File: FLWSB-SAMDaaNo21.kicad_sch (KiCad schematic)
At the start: 29 parts

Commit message: Schema zo goed als af
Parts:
- added D6: D_Schottky, symbol Device:D_Schottky
- added J2: DEBUG, symbol Connector_Generic:Conn_01x03
- added R5, R6: 4.7k, symbol Device:R
- added TP2: VBUS, symbol Connector:TestPoint
- added TP3: VDD, symbol Connector:TestPoint
- added TP4: VIN, symbol Connector:TestPoint
- added TP5: TestPoint, symbol Connector:TestPoint
- J3, J4: renamed from J?; symbol Connector:Conn_01x15_Male -> Connector_Generic:Conn_01x15
- SW1: renamed from SW?; value SW_Push -> SW_RESET
- gave numbers to parts that had none: 26
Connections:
- net 3.3V is gone; now on net +3V3: C4.1, U1.2 (VO)
- net +3V3: now also J3.2 (Pin_2), R5.1, R6.1, TP3.1; no longer J3.14 (Pin_14)
- net GND: now also J3.3 (Pin_3), J4.15 (Pin_15); no longer J3.15 (Pin_15)
- net RESET: now also J2.3 (Pin_3); no longer J3.3 (Pin_3)
- net SERCOM0_PAD0_TX: now also J4.14 (Pin_14); no longer J4.1 (Pin_1)
- net SERCOM0_PAD1_RX: now also J4.13 (Pin_13); no longer J4.2 (Pin_2)
- net SERCOM2_PAD1_TX: now also J4.12 (Pin_12); no longer J4.3 (Pin_3)
- net SERCOM2_PAD2_RX: now also J4.11 (Pin_11); no longer J4.4 (Pin_4)
- net SERCOM3_MISO: now also J4.6 (Pin_6); no longer J4.9 (Pin_9)
- net SERCOM3_MOSI: now also J4.5 (Pin_5); no longer J4.10 (Pin_10)
- net SERCOM3_SCK: now also J4.4 (Pin_4); no longer J4.11 (Pin_11)
- net SERCOM4_PAD0_SDA: now also J4.8 (Pin_8), R5.2; no longer J4.7 (Pin_7)
- net SERCOM4_PAD1_SCL: now also J4.7 (Pin_7), R6.2; no longer J4.8 (Pin_8)
- net SERCOM5_PAD0_TX: now also J4.10 (Pin_10); no longer J4.5 (Pin_5)
- net SERCOM5_PAD1_RX: now also J4.9 (Pin_9); no longer J4.6 (Pin_6)
- net SWCLK: now also J2.1 (Pin_1); no longer J3.1 (Pin_1)
- net SWDIO: now also J2.2 (Pin_2); no longer J3.2 (Pin_2)
- net PA02: now reaches J3.13 (Pin_13)
- net PA02: now also U2.3 (PA02)
- net at U2.39 (PA27): now also TP5.1
- net PB02: now reaches U2.47 (PB02)
- net PB02: now also J3.15 (Pin_15)
- net PB03: now reaches U2.48 (PB03)
- net PB03: now also J3.14 (Pin_14)
- net A0 renamed PA10
- net PA10: now also J3.9 (Pin_9); no longer J4.12 (Pin_12)
- net A1 renamed PA11
- net PA11: now also J3.8 (Pin_8); no longer J4.13 (Pin_13)
- net A2 renamed PA19
- net PA19: now also J3.5 (Pin_5); no longer J4.14 (Pin_14)
- net ADC_0 renamed PA20
- net PA20: now also U2.29 (PA20); no longer U2.3 (PA02)
- net D0 renamed PA03
- net PA03: now also J3.12 (Pin_12); no longer J3.9 (Pin_9)
- net D1 renamed PA09
- net D2 renamed PA06
- net PA06: now also U2.11 (PA06); no longer U2.29 (PA20)
- net D3 renamed PA21
- net PA21: now also J4.1 (Pin_1); no longer J3.12 (Pin_12)
- net PWM0_WO0 renamed PA14
- net PA14: now also J3.7 (Pin_7); no longer J3.5 (Pin_5)
- net PWM0_WO1 renamed PA15
- net PWM1_WO0 renamed PB08
- net PB08: now also J4.2 (Pin_2); no longer J3.7 (Pin_7)
- net PWM1_WO1 renamed PB09
- net PB09: now also J4.3 (Pin_3); no longer J3.8 (Pin_8)
- removed net RN2483_RESET: J4.15 (Pin_15), U2.11 (PA06)
- net VBUS_5V renamed VBUS
- net VBUS: now also D6.2 (A), TP2.1; no longer C1.1, U1.3 (VI)
- new net VIN: C1.1, D6.1 (K), J3.1 (Pin_1), TP4.1, U1.3 (VI)
- no-connect marks 13 -> 10
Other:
- note added: "Input / Ouput"
- note added: "Low Dropout Lineair Regulator"
- note added: "Power Supply Connections"
- note added: "RESET & DEBUG"
- note added: "USB Interface & VIN"
- company: (none) -> AP-Hogeschool
- title: (none) -> Flexible LoRaWAN Sensor Board ATSAMD21
- moved on the sheet: C1, C10, C11, C12, C2, C4, C5, C6, C7, C8, C9, L1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

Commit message: PCB bijna af
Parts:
- removed TP5: TestPoint, symbol Connector:TestPoint
- C3: footprint (none) -> Capacitor_SMD:C_0805_2012Metric_Pad1.18x1.45mm_HandSolder
- D1, D2, D3, D4, D5, R4, R5, R6: footprint (none) -> Resistor_SMD:R_0805_2012Metric_Pad1.20x1.40mm_HandSolder
- D6: footprint (none) -> footprints:SOD-123FL
- J1: footprint USB4085-GF-A_REVA4:GCT_USB4085-GF-A_REVA4 -> footprints:GCT_USB4085-GF-A_REVA4
- J2: footprint (none) -> Connector_PinHeader_2.54mm:PinHeader_1x03_P2.54mm_Vertical
- J3, J4: footprint (none) -> Connector_PinHeader_2.54mm:PinHeader_1x15_P2.54mm_Vertical
- TP1: renamed from TP2; footprint (none) -> TestPoint:TestPoint_Pad_D1.0mm
- TP2: renamed from TP3; footprint (none) -> TestPoint:TestPoint_Pad_D1.0mm
- TP3: renamed from TP4; footprint (none) -> TestPoint:TestPoint_Pad_D1.0mm
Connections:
- net PA02: now also J4.14 (Pin_14); no longer J3.13 (Pin_13)
- net PA03: now also J4.13 (Pin_13); no longer J3.12 (Pin_12)
- net PA06: now also J4.8 (Pin_8); no longer J3.11 (Pin_11)
- net PA09: now also J4.7 (Pin_7); no longer J3.10 (Pin_10)
- net PA10: now also J4.4 (Pin_4); no longer J3.9 (Pin_9)
- net PA11: now also J4.3 (Pin_3); no longer J3.8 (Pin_8)
- net PA14: now also J3.15 (Pin_15); no longer J3.7 (Pin_7)
- net PA15: now also J3.14 (Pin_14); no longer J3.6 (Pin_6)
- net PA19: now also J3.10 (Pin_10); no longer J3.5 (Pin_5)
- net PA20: now also J3.9 (Pin_9); no longer J3.4 (Pin_4)
- net PA21: now also J3.8 (Pin_8); no longer J4.1 (Pin_1)
- net PB03: now also J3.4 (Pin_4); no longer J3.14 (Pin_14)
- net PB08: now also J4.12 (Pin_12); no longer J4.2 (Pin_2)
- net PB09: now also J4.11 (Pin_11); no longer J4.3 (Pin_3)
- net SERCOM0_PAD0_TX: now also J4.10 (Pin_10); no longer J4.14 (Pin_14)
- net SERCOM0_PAD1_RX: now also J4.9 (Pin_9); no longer J4.13 (Pin_13)
- net SERCOM2_PAD1_TX: now also J4.6 (Pin_6); no longer J4.12 (Pin_12)
- net SERCOM2_PAD2_RX: now also J4.5 (Pin_5); no longer J4.11 (Pin_11)
- net SERCOM3_MISO: now also J3.11 (Pin_11); no longer J4.6 (Pin_6)
- net SERCOM3_MOSI: now also J3.13 (Pin_13); no longer J4.5 (Pin_5)
- net SERCOM3_SCK: now also J3.12 (Pin_12); no longer J4.4 (Pin_4)
- net SERCOM4_PAD0_SDA: now also J4.2 (Pin_2); no longer J4.8 (Pin_8)
- net SERCOM4_PAD1_SCL: now also J4.1 (Pin_1); no longer J4.7 (Pin_7)
- net SERCOM5_PAD0_TX: now also J3.7 (Pin_7); no longer J4.10 (Pin_10)
- net SERCOM5_PAD1_RX: now also J3.6 (Pin_6); no longer J4.9 (Pin_9)
- net PB22: now reaches U2.37 (PB22)
- net PB22: now also J3.5 (Pin_5)
- net PB02: no longer names the net of U2.47 (PB02)
- net PB02: no longer J3.15 (Pin_15)
- no-connect marks 10 -> 11

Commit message: Laatste verbeteringen
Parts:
- removed D1, D2, D3, D4, D5: D_Zener, Resistor_SMD:R_0805_2012Metric_Pad1.20x1.40mm_HandSolder, symbol Device:D_Zener
- added C13: 1µF, Capacitor_SMD:C_0805_2012Metric_Pad1.18x1.45mm_HandSolder, symbol Device:C_Small
- added D1: PRTR5V0U2X, Package_TO_SOT_SMD:SOT-143, symbol Power_Protection:PRTR5V0U2X
- added J6: Conn_Coaxial, Connector_Coaxial:U.FL_Molex_MCRF_73412-0110_Vertical, symbol Connector:Conn_Coaxial
- added U3: RN2483, RN2483:RN2483, symbol RN2483:RN2483
- SW1: footprint Button_Switch_SMD:SW_Push_1P1T_NO_6x6mm_H9.5mm -> KMR7_CNK:KMR7_CNK; symbol Switch:SW_Push -> KMR221G-LFS:KMR731NGLFS
- TP1, TP2, TP3: footprint TestPoint:TestPoint_Pad_D1.0mm -> TestPoint:TestPoint_THTPad_1.0x1.0mm_Drill0.5mm
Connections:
- net +3V3: now also C13.2, U3.12 (VDD_1), U3.34 (VDD_2)
- net GND: now also C13.1, D1.1 (GND), J6.2 (Ext), U3.1 (GND_1), U3.11 (GND_3), U3.20 (GND_4), U3.21 (GND_5), U3.22 (GND_6), U3.24 (GND_7), U3.26 (GND_8), U3.27 (GND_9), U3.28 (GND_10), U3.33 (GND_11), U3.41 (GND_12), U3.47 (GND_13), U3.8 (GND_2)
- net SERCOM2_PAD1_TX: now also U3.6 (UART_TX)
- net SERCOM2_PAD2_RX: now also U3.7 (UART_RX)
- net USB+: now also D1.3 (I/O2)
- net USB-: now also D1.2 (I/O1)
- net VBUS: now also D1.4 (VCC)
- net at SW1.1: no longer R1.1
- net PA09 renamed PA07
- net PA10 renamed RN2483_RESET
- net RN2483_RESET: now also U3.32 (~{RESET})
- new net: R1.1, SW1.4
- new net 868MHz: J6.1 (In), U3.23 (RFH)
- no-connect marks 11 -> 41
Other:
- moved on the sheet: C10, C11, C12, C2, C3, C7, C8, C9, D6, J1, L1, R1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

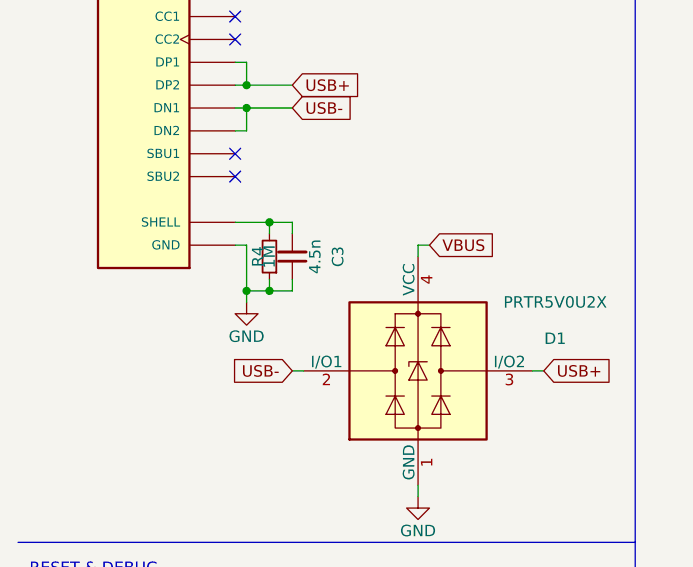
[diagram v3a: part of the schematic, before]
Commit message: USB-C shell aan GND ipv R en C
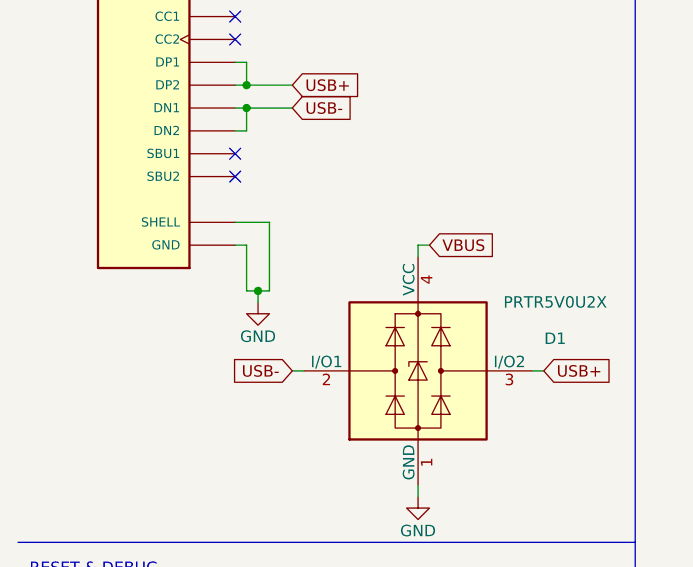
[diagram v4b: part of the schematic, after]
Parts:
- removed C3: 4.5n, Capacitor_SMD:C_0805_2012Metric_Pad1.18x1.45mm_HandSolder, symbol Device:C_Small
- removed R4: 1M, Resistor_SMD:R_0805_2012Metric_Pad1.20x1.40mm_HandSolder, symbol Device:R_Small
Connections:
- net GND: now also J1.P1 (SHELL), J1.P2 (SHELL), J1.P3 (SHELL), J1.P4 (SHELL)
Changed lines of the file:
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@@
     (comment 1 "Bavo, Birk, Daan")
   )
-  (junction (at 39.37 59.69) (diameter 0) (color 0 0 0 0)
-  )
   (junction (at 132.08 161.29) (diameter 0) (color 0 0 0 0)
   )
+  (junction (at 38.1 59.69) (diameter 0) (color 0 0 0 0)
+  )
   (junction (at 62.23 24.13) (diameter 0) (color 0 0 0 0)
   )
@@
   (junction (at 158.75 30.48) (diameter 0) (color 0 0 0 0)
   )
-  (junction (at 39.37 52.07) (diameter 0) (color 0 0 0 0)
-  )
   (junction (at 132.08 27.94) (diameter 0) (color 0 0 0 0)
   )
@@
   )
   (junction (at 166.37 60.96) (diameter 0) (color 0 0 0 0)
-  )
-  (junction (at 36.83 59.69) (diameter 0) (color 0 0 0 0)
   )
   (junction (at 64.77 111.76) (diameter 0) (color 0 0 0 0)
@@
     (stroke (width 0) (type default) (color 0 0 0 0))
   )
-  (wire (pts (xy 41.91 58.42) (xy 41.91 59.69))
-    (stroke (width 0) (type default) (color 0 0 0 0))
-  )
   (wire (pts (xy 33.02 137.16) (xy 34.29 137.16))
     (stroke (width 0) (type default) (color 0 0 0 0))
@@
     (stroke (width 0) (type default) (color 0 0 0 0))
   )
+  (wire (pts (xy 38.1 59.69) (xy 36.83 59.69))
+    (stroke (width 0) (type default) (color 0 0 0 0))
+  )
   (wire (pts (xy 55.88 111.76) (xy 54.61 111.76))
     (stroke (width 0) (type default) (color 0 0 0 0))
@@
     (stroke (width 0) (type default) (color 0 0 0 0))
   )
-  (wire (pts (xy 39.37 52.07) (xy 39.37 53.34))
-    (stroke (width 0) (type default) (color 0 0 0 0))
-  )
-  (wire (pts (xy 39.37 59.69) (xy 36.83 59.69))
+  (wire (pts (xy 39.37 59.69) (xy 38.1 59.69))
     (stroke (width 0) (type default) (color 0 0 0 0))
   )
@@
     (stroke (width 0) (type default) (color 0 0 0 0))
   )
+  (wire (pts (xy 39.37 52.07) (xy 39.37 59.69))
+    (stroke (width 0) (type default) (color 0 0 0 0))
+  )
   (wire (pts (xy 111.76 129.54) (xy 113.03 129.54))
     (stroke (width 0) (type default) (color 0 0 0 0))
@@
     (stroke (width 0) (type default) (color 0 0 0 0))
   )
-  (wire (pts (xy 36.83 59.69) (xy 36.83 60.96))
-    (stroke (width 0) (type default) (color 0 0 0 0))
-  )
   (wire (pts (xy 35.56 52.07) (xy 39.37 52.07))
     (stroke (width 0) (type default) (color 0 0 0 0))
@@
     (stroke (width 0) (type default) (color 0 0 0 0))
   )
-  (wire (pts (xy 41.91 59.69) (xy 39.37 59.69))
-    (stroke (width 0) (type default) (color 0 0 0 0))
-  )
   (wire (pts (xy 22.86 135.89) (xy 22.86 137.16))
     (stroke (width 0) (type default) (color 0 0 0 0))
@@
     (stroke (width 0) (type default) (color 0 0 0 0))
   )
+  (wire (pts (xy 38.1 59.69) (xy 38.1 60.96))
+    (stroke (width 0) (type default) (color 0 0 0 0))
+  )
   (wire (pts (xy 62.23 24.13) (xy 64.77 24.13))
     (stroke (width 0) (type default) (color 0 0 0 0))
@@
     (stroke (width 0) (type default) (color 0 0 0 0))
   )
-  (wire (pts (xy 39.37 52.07) (xy 41.91 52.07))
-    (stroke (width 0) (type default) (color 0 0 0 0))
-  )
   (wire (pts (xy 223.52 77.47) (xy 227.33 77.47))
     (stroke (width 0) (type default) (color 0 0 0 0))
@@
   )
   (polyline (pts (xy 175.26 165.1) (xy 175.26 101.6))
-    (stroke (width 0) (type default) (color 0 0 0 0))
-  )
-  (wire (pts (xy 41.91 52.07) (xy 41.91 53.34))
-    (stroke (width 0) (type default) (color 0 0 0 0))
-  )
-  (wire (pts (xy 39.37 58.42) (xy 39.37 59.69))
     (stroke (width 0) (type default) (color 0 0 0 0))
   )
@@
     )
     (pin "1")
-  )
-  (symbol (lib_id "Device:R_Small") (at 39.37 55.88 180) (unit 1)
-    (in_bom yes) (on_board yes)
-    (property "Reference" "R4" (id 0) (at 38.1 55.88 90))
-    (property "Value" "1M" (id 1) (at 39.37 55.88 90))
-    (property "Footprint" "Resistor_SMD:R_0805_2012Metric_Pad1.20x1.40mm_HandSolder" (id 2) (at 39.37 55.88 0)
-      (effects (font (size 1.27 1.27)) hide)
-    )
-    (property "Datasheet" "~" (id 3) (at 39.37 55.88 0)
-      (effects (font (size 1.27 1.27)) hide)
-    )
-    (pin "1")
-    (pin "2")
   )
   (symbol (lib_id "Device:C_Small") (at 179.07 49.53 180) (unit 1)
@@
     (pin "1")
   )
-  (symbol (lib_id "Device:C_Small") (at 41.91 55.88 180) (unit 1)
-    (in_bom yes) (on_board yes)
-    (property "Reference" "C3" (id 0) (at 46.99 55.88 90))
-    (property "Value" "4.5n" (id 1) (at 44.45 55.88 90))
-    (property "Footprint" "Capacitor_SMD:C_0805_2012Metric_Pad1.18x1.45mm_HandSolder" (id 2) (at 41.91 55.88 0)
-      (effects (font (size 1.27 1.27)) hide)
-    )
-    (property "Datasheet" "~" (id 3) (at 41.91 55.88 0)
-      (effects (font (size 1.27 1.27)) hide)
-    )
-    (pin "1")
-    (pin "2")
-  )
   (symbol (lib_id "Device:C_Polarized_Small") (at 29.21 175.26 0) (unit 1)
     (in_bom yes) (on_board yes) (fields_autoplaced)
@@
     (pin "2")
   )
-  (symbol (lib_id "power:GND") (at 36.83 60.96 0) (unit 1)
+  (symbol (lib_id "power:GND") (at 38.1 60.96 0) (unit 1)
     (in_bom yes) (on_board yes)
-    (property "Reference" "#PWR04" (id 0) (at 36.83 67.31 0)
-      (effects (font (size 1.27 1.27)) hide)
-    )
-    (property "Value" "GND" (id 1) (at 36.83 64.77 0))
-    (property "Footprint" "" (id 2) (at 36.83 60.96 0)
-      (effects (font (size 1.27 1.27)) hide)
-    )
-    (property "Datasheet" "" (id 3) (at 36.83 60.96 0)
+    (property "Reference" "#PWR04" (id 0) (at 38.1 67.31 0)
+      (effects (font (size 1.27 1.27)) hide)
+    )
+    (property "Value" "GND" (id 1) (at 38.1 64.77 0))
+    (property "Footprint" "" (id 2) (at 38.1 60.96 0)
+      (effects (font (size 1.27 1.27)) hide)
+    )
+    (property "Datasheet" "" (id 3) (at 38.1 60.96 0)
       (effects (font (size 1.27 1.27)) hide)
     )
@@
       (reference "C2") (unit 1) (value "100nF") (footprint "Capacitor_SMD:C_0805_2012Metric_Pad1.18x1.45mm_HandSolder")
     )
-    (path "/3f6206c6-ce20-4874-8734-b61d42c7649d"
-      (reference "C3") (unit 1) (value "4.5n") (footprint "Capacitor_SMD:C_0805_2012Metric_Pad1.18x1.45mm_HandSolder")
-    )
     (path "/cb9a1690-2ab2-473c-a6ca-adf74e511205"
       (reference "C4") (unit 1) (value "10µF") (footprint "Capacitor_SMD:C_0805_2012Metric_Pad1.18x1.45mm_HandSolder")
@@
       (reference "R3") (unit 1) (value "10k") (footprint "Resistor_SMD:R_0805_2012Metric_Pad1.20x1.40mm_HandSolder")
     )
-    (path "/32b1c68c-fd93-441e-944d-342d9fd9b8e7"
-      (reference "R4") (unit 1) (value "1M") (footprint "Resistor_SMD:R_0805_2012Metric_Pad1.20x1.40mm_HandSolder")
-    )
     (path "/473553e0-010f-4e3d-ad77-84ae3ea91407"
